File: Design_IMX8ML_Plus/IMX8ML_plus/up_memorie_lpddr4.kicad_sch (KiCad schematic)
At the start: 10 parts, among them U1 MIMX8ML8CVNKZAB, U2 MT53E1536M32D4DT-046 WT:A

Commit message: Add Base board IMxM8ML project
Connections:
- net ECSPI1_MOSI: now reaches U1.AC20 (ECSPI1_MOSI)
- net ECSPI1_MISO: now reaches U1.AD20 (ECSPI1_MISO)
- net ECSPI1_SSO: now reaches U1.AE20 (ECSPI1_SS0)
- net ECSPI1_SCLK: now reaches U1.AF20 (ECSPI1_SCLK)
- net ECSPI2_MISO: now reaches U1.AH20 (ECSPI2_MISO)
- net ECSPI2_SCLK: now reaches U1.AH21 (ECSPI2_SCLK)
- net EARC_N_HPD: now reaches U1.AH22 (EARC_N_HPD)
- net EARC_AUX: now reaches U1.AH23 (EARC_AUX)
- net ECSPI2_MOSI: now reaches U1.AJ21 (ECSPI2_MOSI)
- net ECSPI2_SSO: now reaches U1.AJ22 (ECSPI2_SS0)
- net EARC_P_UTIL: now reaches U1.AJ23 (EARC_P_UTIL)
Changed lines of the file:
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@@
+    (stroke (width 0) (type default))
+  )
+  (wire (pts (xy 254 124.46) (xy 262.89 124.46))
     (stroke (width 0) (type default))
   )
@@
     (stroke (width 0) (type default))
   )
+  (wire (pts (xy 254 137.16) (xy 262.89 137.16))
+    (stroke (width 0) (type default))
+  )
   (wire (pts (xy 166.37 27.94) (xy 157.48 27.94))
     (stroke (width 0) (type default))
@@
     (stroke (width 0) (type default))
   )
+  (wire (pts (xy 254 144.78) (xy 262.89 144.78))
+    (stroke (width 0) (type default))
+  )
   (wire (pts (xy 101.6 177.8) (xy 83.82 177.8))
     (stroke (width 0) (type default))
@@
     (stroke (width 0) (type default))
   )
+  (wire (pts (xy 254 129.54) (xy 262.89 129.54))
+    (stroke (width 0) (type default))
+  )
   (wire (pts (xy 179.07 58.42) (xy 196.85 58.42))
     (stroke (width 0) (type default))
@@
     (stroke (width 0) (type default))
   )
+  (wire (pts (xy 254 119.38) (xy 262.89 119.38))
+    (stroke (width 0) (type default))
+  )
   (wire (pts (xy 62.23 24.13) (xy 59.69 24.13))
     (stroke (width 0) (type default))
@@
     (stroke (width 0) (type default))
   )
+  (wire (pts (xy 254 134.62) (xy 262.89 134.62))
+    (stroke (width 0) (type default))
+  )
   (wire (pts (xy 96.52 82.55) (xy 78.74 82.55))
     (stroke (width 0) (type default))
   )
+  (wire (pts (xy 254 139.7) (xy 262.89 139.7))
+    (stroke (width 0) (type default))
+  )
   (wire (pts (xy 101.6 182.88) (xy 83.82 182.88))
     (stroke (width 0) (type default))
@@
     (stroke (width 0) (type default))
   )
+  (wire (pts (xy 254 147.32) (xy 262.89 147.32))
+    (stroke (width 0) (type default))
+  )
   (wire (pts (xy 101.6 180.34) (xy 83.82 180.34))
     (stroke (width 0) (type default))
@@
     (stroke (width 0) (type default))
   )
+  (wire (pts (xy 254 132.08) (xy 262.89 132.08))
+    (stroke (width 0) (type default))
+  )
   (wire (pts (xy 101.6 167.64) (xy 83.82 167.64))
     (stroke (width 0) (type default))
@@
     (stroke (width 0) (type default))
   )
+  (wire (pts (xy 254 142.24) (xy 262.89 142.24))
+    (stroke (width 0) (type default))
+  )
   (wire (pts (xy 171.45 27.94) (xy 196.85 27.94))
     (stroke (width 0) (type default))
@@
     (stroke (width 0) (type default))
   )
+  (wire (pts (xy 254 121.92) (xy 262.89 121.92))
+    (stroke (width 0) (type default))
+  )
   (label "DRAM_DATA5_A" (at 179.07 149.86 0) (fields_autoplaced)
     (effects (font (size 1.27 1.27)) (justify left bottom))
@@
     (effects (font (size 1.27 1.27)) (justify left bottom))
   )
+  (global_label "EARC_N_HPD" (shape input) (at 262.89 121.92 0) (fields_autoplaced)
+    (effects (font (size 1 1)) (justify left))
+    (property "Intersheetrefs" "${INTERSHEET_REFS}" (at 274.5588 121.92 0)
+      (effects (font (size 1.27 1.27)) (justify left) hide)
+    )
+  )
+  (global_label "ECSPI2_MOSI" (shape input) (at 262.89 142.24 0) (fields_autoplaced)
+    (effects (font (size 1 1)) (justify left))
+    (property "Intersheetrefs" "${INTERSHEET_REFS}" (at 274.8447 142.24 0)
+      (effects (font (size 1.27 1.27)) (justify left) hide)
+    )
+  )
+  (global_label "ECSPI2_SSO" (shape input) (at 262.89 147.32 0) (fields_autoplaced)
+    (effects (font (size 1 1)) (justify left))
+    (property "Intersheetrefs" "${INTERSHEET_REFS}" (at 274.178 147.32 0)
+      (effects (font (size 1.27 1.27)) (justify left) hide)
+    )
+  )
   (global_label "VDD_1V8" (shape input) (at 57.15 21.59 90) (fields_autoplaced)
     (effects (font (size 1 1)) (justify left))
@@
     (effects (font (size 1 1)) (justify left))
     (property "Intersheetrefs" "${INTERSHEET_REFS}" (at 76.7083 24.13 0)
+      (effects (font (size 1.27 1.27)) (justify left) hide)
+    )
+  )
+  (global_label "EARC_P_UTIL" (shape input) (at 262.89 124.46 0) (fields_autoplaced)
+    (effects (font (size 1 1)) (justify left))
+    (property "Intersheetrefs" "${INTERSHEET_REFS}" (at 274.5588 124.46 0)
+      (effects (font (size 1.27 1.27)) (justify left) hide)
+    )
+  )
+  (global_label "EARC_AUX" (shape input) (at 262.89 119.38 0) (fields_autoplaced)
+    (effects (font (size 1 1)) (justify left))
+    (property "Intersheetrefs" "${INTERSHEET_REFS}" (at 272.5588 119.38 0)
+      (effects (font (size 1.27 1.27)) (justify left) hide)
+    )
+  )
+  (global_label "ECSPI1_SCLK" (shape input) (at 262.89 134.62 0) (fields_autoplaced)
+    (effects (font (size 1 1)) (justify left))
+    (property "Intersheetrefs" "${INTERSHEET_REFS}" (at 274.9875 134.62 0)
       (effects (font (size 1.27 1.27)) (justify left) hide)
     )
@@
     )
   )
+  (global_label "ECSPI2_MISO" (shape input) (at 262.89 139.7 0) (fields_autoplaced)
+    (effects (font (size 1 1)) (justify left))
+    (property "Intersheetrefs" "${INTERSHEET_REFS}" (at 274.8447 139.7 0)
+      (effects (font (size 1.27 1.27)) (justify left) hide)
+    )
+  )
+  (global_label "ECSPI1_MOSI" (shape input) (at 262.89 132.08 0) (fields_autoplaced)
+    (effects (font (size 1 1)) (justify left))
+    (property "Intersheetrefs" "${INTERSHEET_REFS}" (at 274.8447 132.08 0)
+      (effects (font (size 1.27 1.27)) (justify left) hide)
+    )
+  )
+  (global_label "ECSPI1_MISO" (shape input) (at 262.89 129.54 0) (fields_autoplaced)
+    (effects (font (size 1 1)) (justify left))
+    (property "Intersheetrefs" "${INTERSHEET_REFS}" (at 274.8447 129.54 0)
+      (effects (font (size 1.27 1.27)) (justify left) hide)
+    )
+  )
+  (global_label "ECSPI2_SCLK" (shape input) (at 262.89 144.78 0) (fields_autoplaced)
+    (effects (font (size 1 1)) (justify left))
+    (property "Intersheetrefs" "${INTERSHEET_REFS}" (at 274.9875 144.78 0)
+      (effects (font (size 1.27 1.27)) (justify left) hide)
+    )
+  )
+  (global_label "ECSPI1_SSO" (shape input) (at 262.89 137.16 0) (fields_autoplaced)
+    (effects (font (size 1 1)) (justify left))
+    (property "Intersheetrefs" "${INTERSHEET_REFS}" (at 274.178 137.16 0)
+      (effects (font (size 1.27 1.27)) (justify left) hide)
+    )
+  )

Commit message: CPU Board actualizate
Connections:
- net DRAM_CA6_A: now reaches U1.G4 (DRAM_AC06)
- net DRAM_CA7_A: now reaches U1.J5 (DRAM_AC07)
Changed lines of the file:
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@@
+	(wire
+		(pts
+			(xy 179.07 45.72) (xy 196.85 45.72)
+		)
+		(stroke
+			(width 0)
+			(type default)
+		)
+	)
 	(wire
 		(pts
@@
 		(pts
 			(xy 179.07 139.7) (xy 196.85 139.7)
+		)
+		(stroke
+			(width 0)
+			(type default)
+		)
+	)
+	(wire
+		(pts
+			(xy 179.07 43.18) (xy 196.85 43.18)
 		)
 		(stroke
@@
 		)
 	)
+	(label "DRAM_CA6_A"
+		(at 179.07 43.18 0)
+		(effects
+			(font
+				(size 1.27 1.27)
+			)
+			(justify left bottom)
+		)
+	)
 	(label "DRAM_CA4_A"
 		(at 101.6 151.13 180)
@@
 		(effects
 			(font
+				(size 1.27 1.27)
+			)
+			(justify left bottom)
+		)
+	)
+	(label "DRAM_CA7_A"
+		(at 179.07 45.72 0)
+		(effects
+			(font

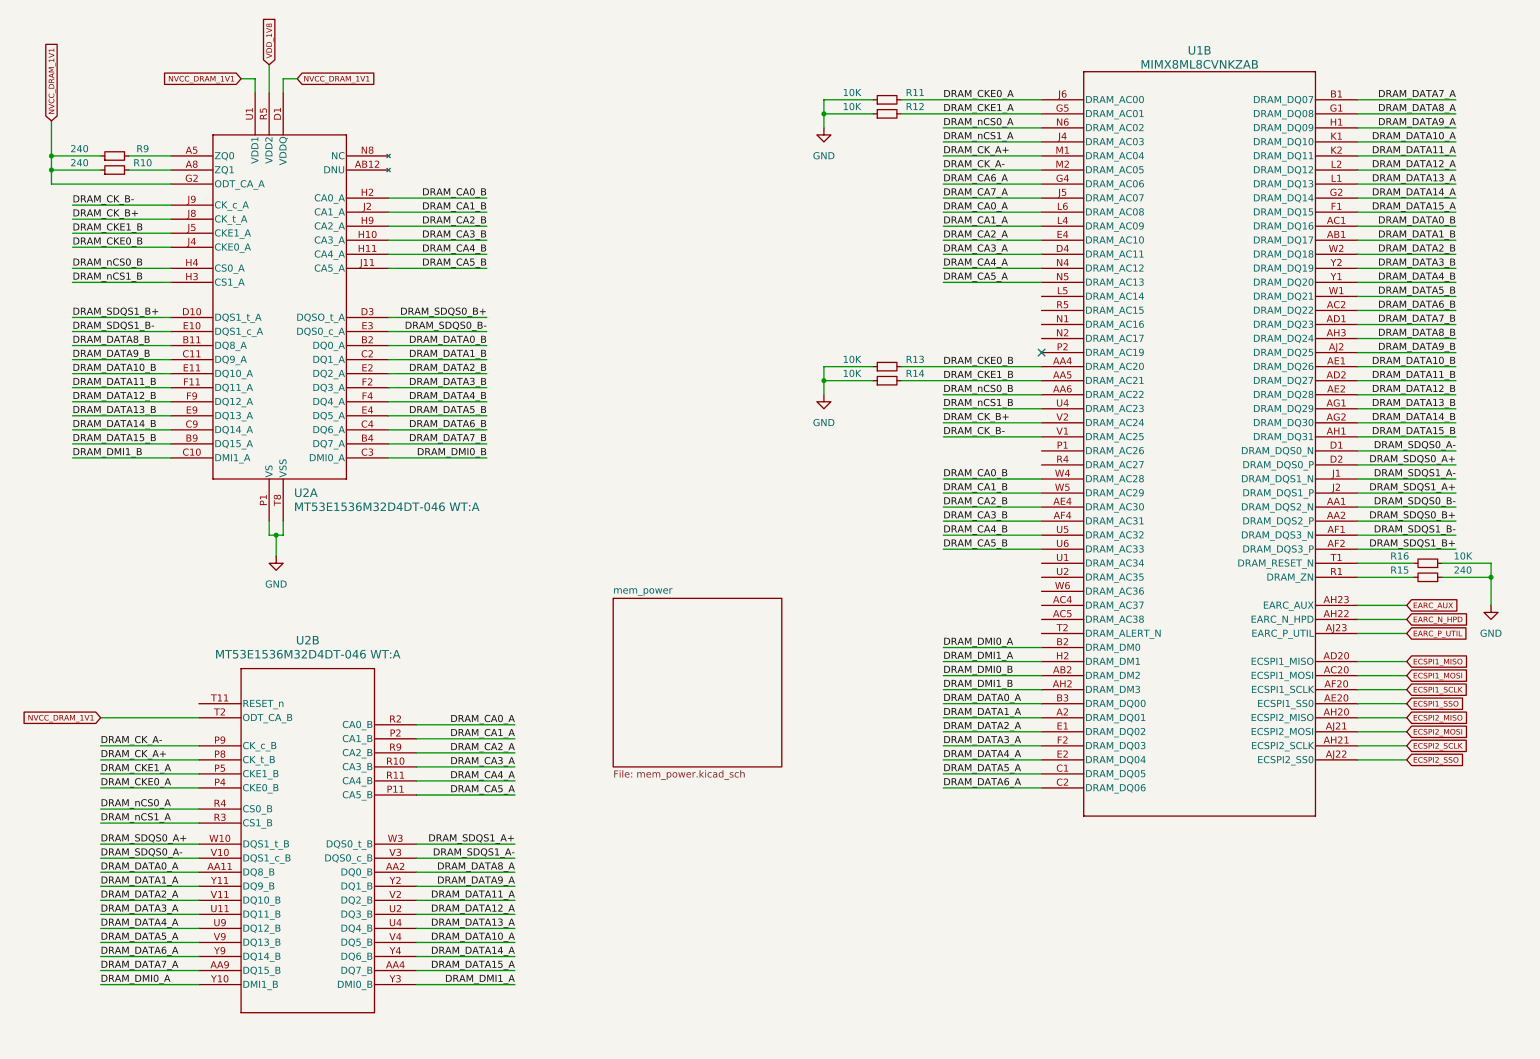
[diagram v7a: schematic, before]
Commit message: [IMX8ML-Processor] Reorganization of the pinout conector since processor to conectors
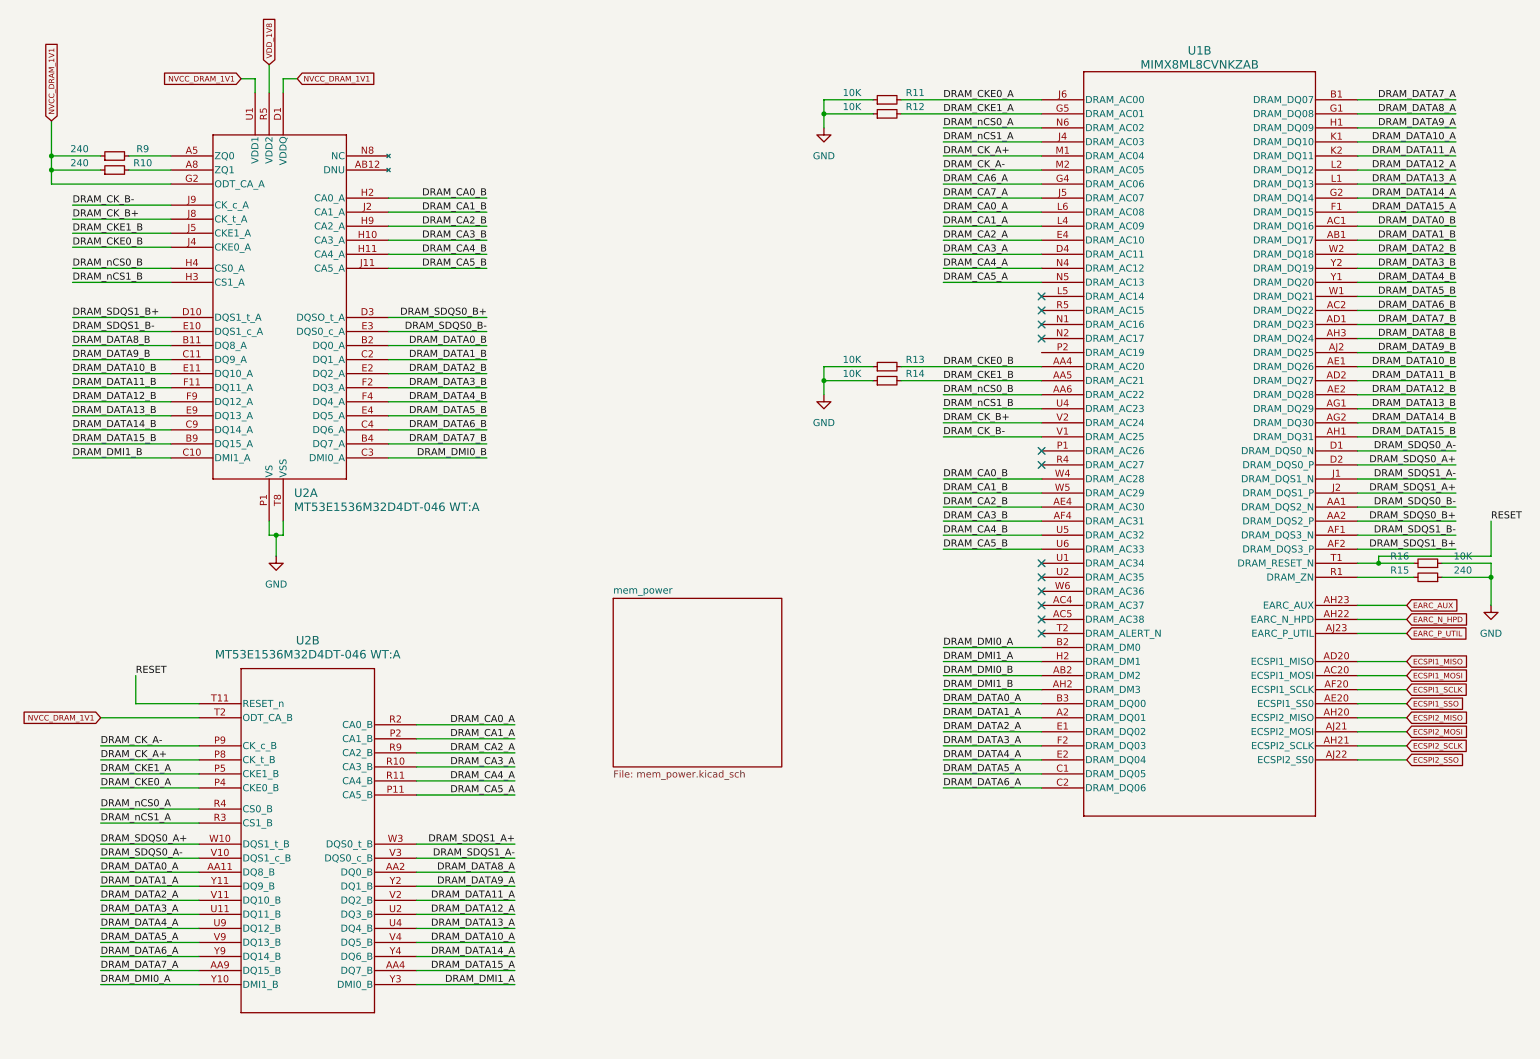
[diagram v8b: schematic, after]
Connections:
- net RESET: now reaches R16.2, U1.T1 (DRAM_RESET_N)
- net RESET: now also U2.T11 (RESET_n)
- no-connect marks 1 -> 12
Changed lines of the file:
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@@
+	)
+	(junction
+		(at 257.81 111.76)
+		(diameter 0)
+		(color 0 0 0 0)
 	)
 	(junction
@@
 	)
 	(no_connect
-		(at 196.85 73.66)
+		(at 196.85 71.12)
+	)
+	(no_connect
+		(at 196.85 121.92)
+	)
+	(no_connect
+		(at 196.85 114.3)
+	)
+	(no_connect
+		(at 196.85 116.84)
+	)
+	(no_connect
+		(at 196.85 124.46)
+	)
+	(no_connect
+		(at 196.85 93.98)
+	)
+	(no_connect
+		(at 196.85 119.38)
+	)
+	(no_connect
+		(at 196.85 66.04)
+	)
+	(no_connect
+		(at 196.85 91.44)
+	)
+	(no_connect
+		(at 196.85 68.58)
+	)
+	(no_connect
+		(at 196.85 63.5)
+	)
+	(no_connect
+		(at 196.85 111.76)
 	)
 	(wire
@@
 	(wire
 		(pts
-			(xy 264.16 111.76) (xy 254 111.76)
+			(xy 264.16 111.76) (xy 257.81 111.76)
 		)
 		(stroke
@@
 	(wire
 		(pts
+			(xy 33.02 132.08) (xy 33.02 137.16)
+		)
+		(stroke
+			(width 0)
+			(type default)
+		)
+	)
+	(wire
+		(pts
 			(xy 271.78 91.44) (xy 254 91.44)
 		)
@@
 	(wire
 		(pts
+			(xy 257.81 111.76) (xy 254 111.76)
+		)
+		(stroke
+			(width 0)
+			(type default)
+		)
+	)
+	(wire
+		(pts
 			(xy 157.48 30.48) (xy 157.48 33.02)
 		)
@@
 	(wire
 		(pts
+			(xy 278.13 104.14) (xy 278.13 110.49)
+		)
+		(stroke
+			(width 0)
+			(type default)
+		)
+	)
+	(wire
+		(pts
 			(xy 21.59 60.96) (xy 39.37 60.96)
 		)
@@
 	(wire
 		(pts
+			(xy 257.81 110.49) (xy 278.13 110.49)
+		)
+		(stroke
+			(width 0)
+			(type default)
+		)
+	)
+	(wire
+		(pts
 			(xy 26.67 177.8) (xy 44.45 177.8)
 		)
@@
 	(wire
 		(pts
+			(xy 257.81 111.76) (xy 257.81 110.49)
+		)
+		(stroke
+			(width 0)
+			(type default)
+		)
+	)
+	(wire
+		(pts
 			(xy 54.61 24.13) (xy 54.61 26.67)
 		)
@@
 		(pts
 			(xy 101.6 167.64) (xy 83.82 167.64)
+		)
+		(stroke
+			(width 0)
+			(type default)
+		)
+	)
+	(wire
+		(pts
+			(xy 44.45 137.16) (xy 33.02 137.16)
 		)
 		(stroke
@@
 		)
 	)
+	(label "RESET"
+		(at 33.02 132.08 0)
+		(effects
+			(font
+				(size 1.27 1.27)
+			)
+			(justify left bottom)
+		)
+	)
 	(label "DRAM_SDQS0_A+"
 		(at 271.78 93.98 180)
@@
 		(effects
 			(font
+				(size 1.27 1.27)
+			)
+			(justify left bottom)
+		)
+	)
+	(label "RESET"
+		(at 278.13 104.14 0)
+		(effects
+			(font
